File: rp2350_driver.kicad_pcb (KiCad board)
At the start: 6 copper layers, 76 x 46.4 mm, 291 parts, among them J1 XT30, J10 Power Output, J11 CAN2 PLUG, J12 Conn_01x06, J2 XT30, J3 USB_C_Receptacle_USB2.0, J4 SM03B-SRSS-TB, J5 Estop Conn, J6 SM03B-SRSS-TB, J7 Conn_01x03, J8 Conn_01x03, J9 XT30, Q1 Q_PNP_BEC, Q2 Q_PNP_BEC, Q3 Q_PNP_BEC, Q4 Q_PNP_BEC, Q5 Q_NMOS_GDS, SW1 Button, SW2 Button, U1 EG3113, U10 INA240A1D, U101 FUSB302BMPX, U11 USBLC6-2P6, U12 EG3113, U13 TS5A3159DCK, U14 TS5A3159DCK, U15 TS5A3159DCK, U16 CA-IS3052CG, U17 TS5A3159DCK, U18 SIT3088ETK, U19 SIT3088ETK, U20 SIT3088ETK, U21 SIT3088ETK, U22 TS5A3159DCK, U23 TS5A3159DCK, U24 TS5A3159DCK, U25 TS5A3159DCK, U26 TS5A3159DCK, U27 TS5A3159DCK, U28 XL7005A, U29 LM74700, U3 W25Q16JV, U4 SPX3819M5-L-3-3, U5 INA240A1D, U6 EG3113, U7 EG3113, U8 RP2350_80QFN, U9 INA240A1D, Y1 ABM8-272-T3

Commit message: Fix a few parts as per corrections made during order.
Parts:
- C42, C80: value 220uF 63V solid -> 100uF 100V
- R82: value 100R 0402 -> 100R
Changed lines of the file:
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@@
 			)
 		)
-		(property "LCSC" "C14663"
+		(property "LCSC" "C131394"
 			(at 0 0 315)
 			(unlocked yes)
@@
 			)
 		)
-		(property "LCSC" "C14663"
+		(property "LCSC" "C131394"
 			(at 0 0 270)
 			(unlocked yes)
@@
 			)
 		)
-		(property "Value" "220uF 63V solid"
+		(property "Value" "100uF 100V"
 			(at 2.5 6.249999 45)
 			(layer "F.Fab")
@@
 			)
 		)
-		(property "LCSC" "C5455531"
+		(property "LCSC" "C2887236"
 			(at 0 0 45)
 			(layer "F.Fab")
@@
 			)
 		)
-		(property "Value" "220uF 63V solid"
+		(property "Value" "100uF 100V"
 			(at 2.5 6.250001 105)
 			(layer "F.Fab")
@@
 			)
 		)
-		(property "LCSC" "C5455531"
+		(property "LCSC" "C2887236"
 			(at 0 0 285)
 			(unlocked yes)
@@
 			)
 		)
-		(property "LCSC" "C14663"
+		(property "LCSC" "C131394"
 			(at 0 0 0)
 			(unlocked yes)
@@
 			)
 		)
-		(property "LCSC" "C14663"
+		(property "LCSC" "C131394"
 			(at 0 0 270)
 			(unlocked yes)
@@
 			)
 		)
-		(property "LCSC" "C14663"
+		(property "LCSC" "C131394"
 			(at 0 0 180)
 			(unlocked yes)
@@
 			)
 		)
-		(property "LCSC" "C14663"
+		(property "LCSC" "C131394"
 			(at 0 0 90)
 			(unlocked yes)
@@
 			)
 		)
-		(property "LCSC" "C14663"
+		(property "LCSC" "C131394"
 			(at 0 0 90)
 			(unlocked yes)
@@
 			)
 		)
-		(property "LCSC" "C14663"
+		(property "LCSC" "C131394"
 			(at 0 0 90)
 			(unlocked yes)
@@
 			)
 		)
-		(property "LCSC" "C14663"
+		(property "LCSC" "C131394"
 			(at 0 0 270)
 			(unlocked yes)
@@
 			)
 		)
-		(property "LCSC" "C14663"
+		(property "LCSC" "C131394"
 			(at 0 0 180)
 			(unlocked yes)
@@
 			)
 		)
-		(property "Value" "100R 0402"
+		(property "Value" "100R"
 			(at 0 -1.17 90)
 			(layer "B.Fab")
@@
 			)
 		)
-		(property "LCSC" "C14663"
+		(property "LCSC" "C131394"
 			(at 0 0 270)
 			(unlocked yes)
@@
 			)
 		)
-		(property "LCSC" "C14663"
+		(property "LCSC" "C131394"
 			(at 0 0 270)
 			(unlocked yes)
@@
 			)
 		)
-		(property "LCSC" "C14663"
+		(property "LCSC" "C131394"
 			(at 0 0 270)
 			(unlocked yes)
@@
 			)
 		)
-		(property "LCSC" "C14663"
+		(property "LCSC" "C131394"
 			(at 0 0 0)
 			(unlocked yes)
@@
 			)
 		)
-		(property "LCSC" "C14663"
+		(property "LCSC" "C131394"
 			(at 0 0 180)
 			(unlocked yes)

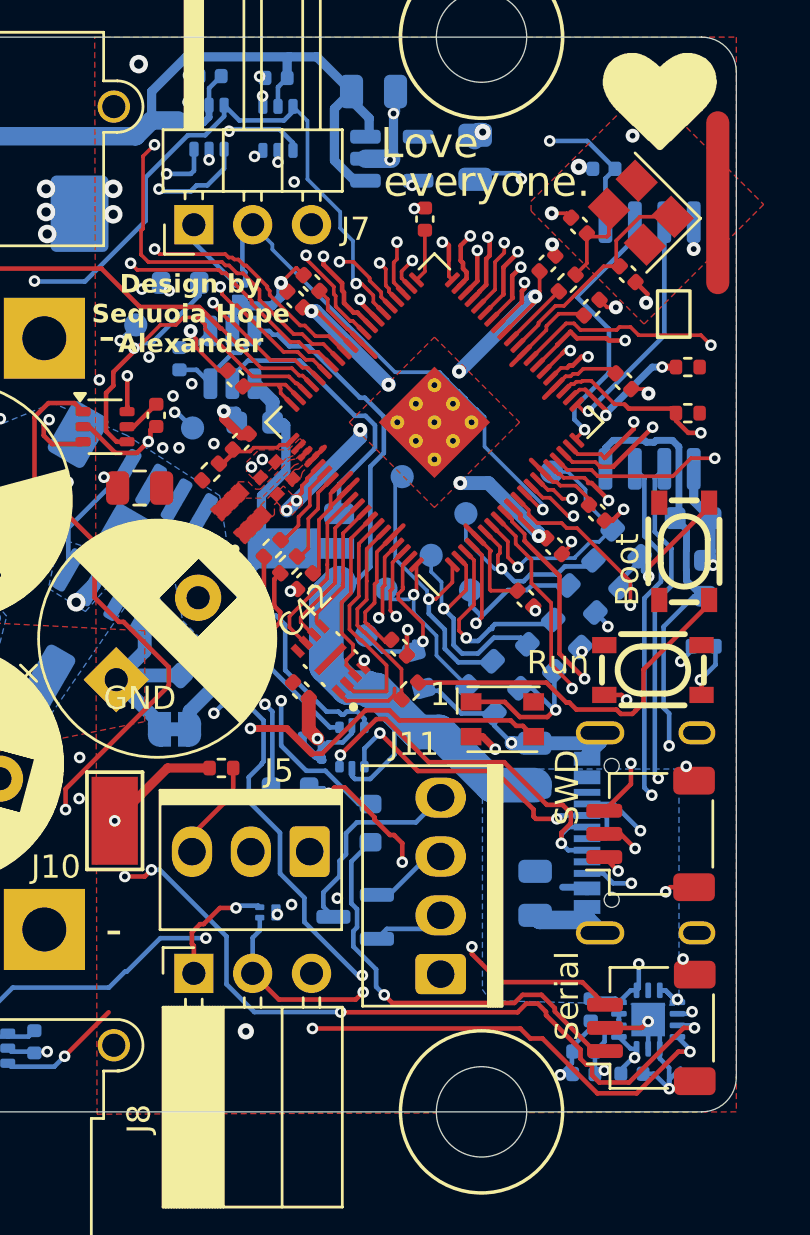
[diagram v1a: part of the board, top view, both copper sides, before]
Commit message: Add encoder plus updated motor driver files.
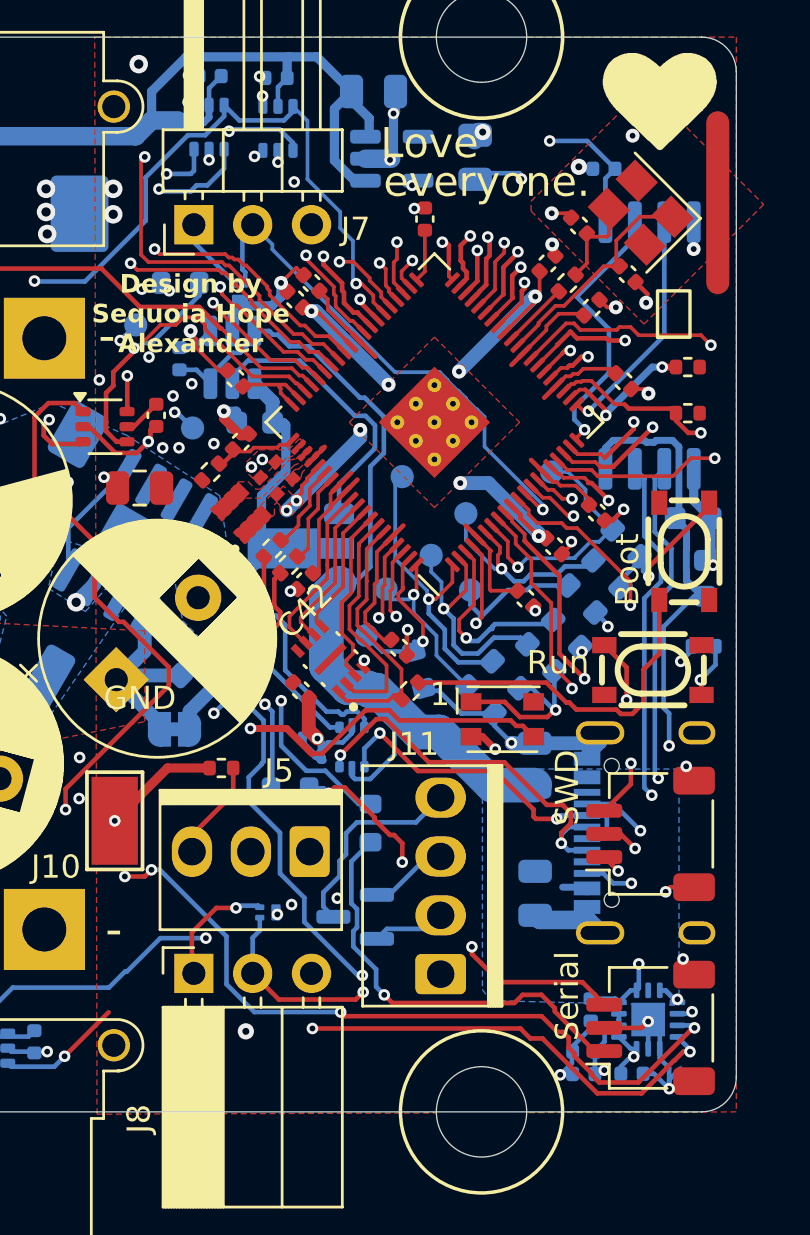
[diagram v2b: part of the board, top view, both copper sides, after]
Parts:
- R20, R23, R39, R40, R55, R56: value 3mΩ -> 8mΩ
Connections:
- SW1 pad 2: /~{USB_BOOT} -> unconnected-(SW1-Pad2)
- SW1 pad 3: (no net) -> unconnected-(SW1-K-Pad3)
- SW1 pad 4: (no net) -> /~{USB_BOOT}
- SW2 pad 2: /RUN -> unconnected-(SW2-Pad2)
- SW2 pad 3: (no net) -> unconnected-(SW2-K-Pad3)
- SW2 pad 4: (no net) -> /RUN
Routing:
- net /RUN: track 30.5 -> 32.2 mm
- net C_SENSE: track 61.3 -> 59.7 mm
- net /~{USB_BOOT}: track 16.1 -> 15.2 mm
- net /I2C_SCL: track 116.1 -> 115.6 mm
